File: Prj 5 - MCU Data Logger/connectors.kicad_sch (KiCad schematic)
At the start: 4 parts, among them J1 Conn_01x04_Pin, J2 Conn_01x04_Pin, J3 Conn_01x09_Pin, J4 Conn_02x03_Odd_Even

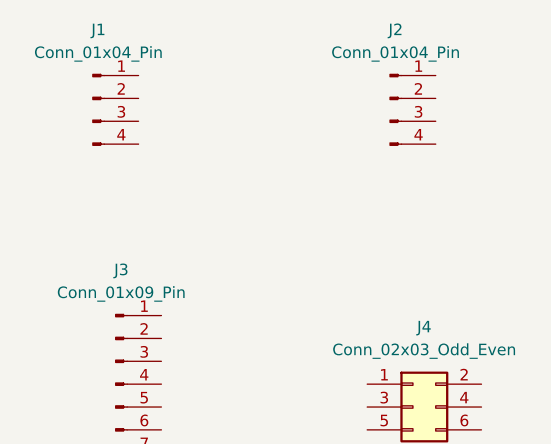
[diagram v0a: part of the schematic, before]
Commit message: wired first main sheet
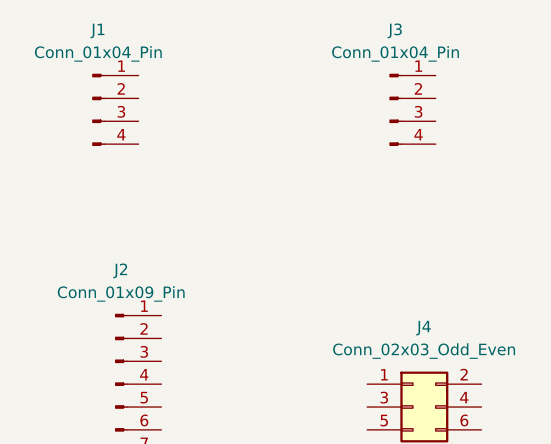
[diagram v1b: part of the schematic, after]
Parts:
- renumbered J3 to J2, J2 to J3
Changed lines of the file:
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@@
 		(dnp no)
 		(fields_autoplaced yes)
-		(property "Reference" "J2"
+		(property "Reference" "J3"
 			(at 95.885 34.29 0)
 			(effects
@@
 			(project "MCU Data Logger"
 				(path "/9e6b6f4b-c9cd-4b00-ba0a-ee2ed324f710/69ef4e9c-8fa8-4a08-a09c-5eb67d38f86d"
-					(reference "J2")
+					(reference "J3")
 					(unit 1)
 				)
@@
 		(dnp no)
 		(fields_autoplaced yes)
-		(property "Reference" "J3"
+		(property "Reference" "J2"
 			(at 65.405 60.96 0)
 			(effects
@@
 			(project ""
 				(path "/9e6b6f4b-c9cd-4b00-ba0a-ee2ed324f710/69ef4e9c-8fa8-4a08-a09c-5eb67d38f86d"
-					(reference "J3")
+					(reference "J2")
 					(unit 1)
 				)

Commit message: Complete wiring, ERC Clean
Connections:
- net GND: now reaches J3.1 (Pin_1)
- net GND: now also J1.1 (Pin_1), J2.8 (Pin_8), J4.6 (Pin_6)
- net BVcc: now reaches J3.2 (Pin_2)
- net BVcc: now also J1.2 (Pin_2), J2.9 (Pin_9), J4.2 (Pin_2)
- net RX: now reaches J3.3 (Pin_3)
- net TX: now reaches J3.4 (Pin_4)
- net D2: now reaches J2.1 (Pin_1)
- net D3: now reaches J2.2 (Pin_2)
- net D4: now reaches J2.3 (Pin_3)
- net D5: now reaches J2.4 (Pin_4)
- net D6: now reaches J2.5 (Pin_5)
- net D7: now reaches J2.6 (Pin_6)
- net D8: now reaches J2.7 (Pin_7)
- net MISO: now reaches J4.1 (Pin_1)
- net SCK: now reaches J4.3 (Pin_3)
- net SCK: now also J1.4 (Pin_4)
- net MOSI: now reaches J4.4 (Pin_4)
- net RESET: now reaches J4.5 (Pin_5)
- net SDA: now reaches J1.3 (Pin_3)
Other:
- note added: "Connectors"
- company: (none) -> AllOkay Solutions
- title: (none) -> Connectors
- moved on the sheet: J1, J2, J3, J4

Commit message: Associated footprints
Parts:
- J1, J3: footprint (none) -> Connector_PinHeader_2.54mm:PinHeader_1x04_P2.54mm_Vertical
- J2: footprint (none) -> Connector_PinHeader_2.54mm:PinHeader_1x09_P2.54mm_Vertical
- J4: footprint (none) -> Connector_PinHeader_2.54mm:PinHeader_2x03_P2.54mm_Vertical
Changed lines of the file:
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@@
 			)
 		)
-		(property "Footprint" ""
+		(property "Footprint" "Connector_PinHeader_2.54mm:PinHeader_1x04_P2.54mm_Vertical"
 			(at 153.67 68.58 0)
 			(effects
@@
 			)
 		)
-		(property "Footprint" ""
+		(property "Footprint" "Connector_PinHeader_2.54mm:PinHeader_1x09_P2.54mm_Vertical"
 			(at 120.65 102.87 0)
 			(effects
@@
 			)
 		)
-		(property "Footprint" ""
+		(property "Footprint" "Connector_PinHeader_2.54mm:PinHeader_2x03_P2.54mm_Vertical"
 			(at 160.02 102.87 0)
 			(effects
@@
 			)
 		)
-		(property "Footprint" ""
+		(property "Footprint" "Connector_PinHeader_2.54mm:PinHeader_1x04_P2.54mm_Vertical"
 			(at 120.65 68.58 0)
 			(effects

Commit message: Separated SCL and SCK
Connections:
- net SCK: no longer J1.4 (Pin_4)
- new net SCL: J1.4 (Pin_4)
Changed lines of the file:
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@@
 		)
 	)
-	(hierarchical_label "SCK"
+	(hierarchical_label "SCL"
 		(shape passive)
 		(at 128.27 73.66 0)
